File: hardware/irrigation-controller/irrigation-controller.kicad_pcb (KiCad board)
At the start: 2 copper layers, 109 x 71.6 mm, 84 parts, among them J1 RS485, J10 I2C, J11 IO, J12 RELAY_2, J15 FLOW_1, J2 I2C, J3 ICSP, J4 UART, J5 RF Module, J6 PWR 24V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

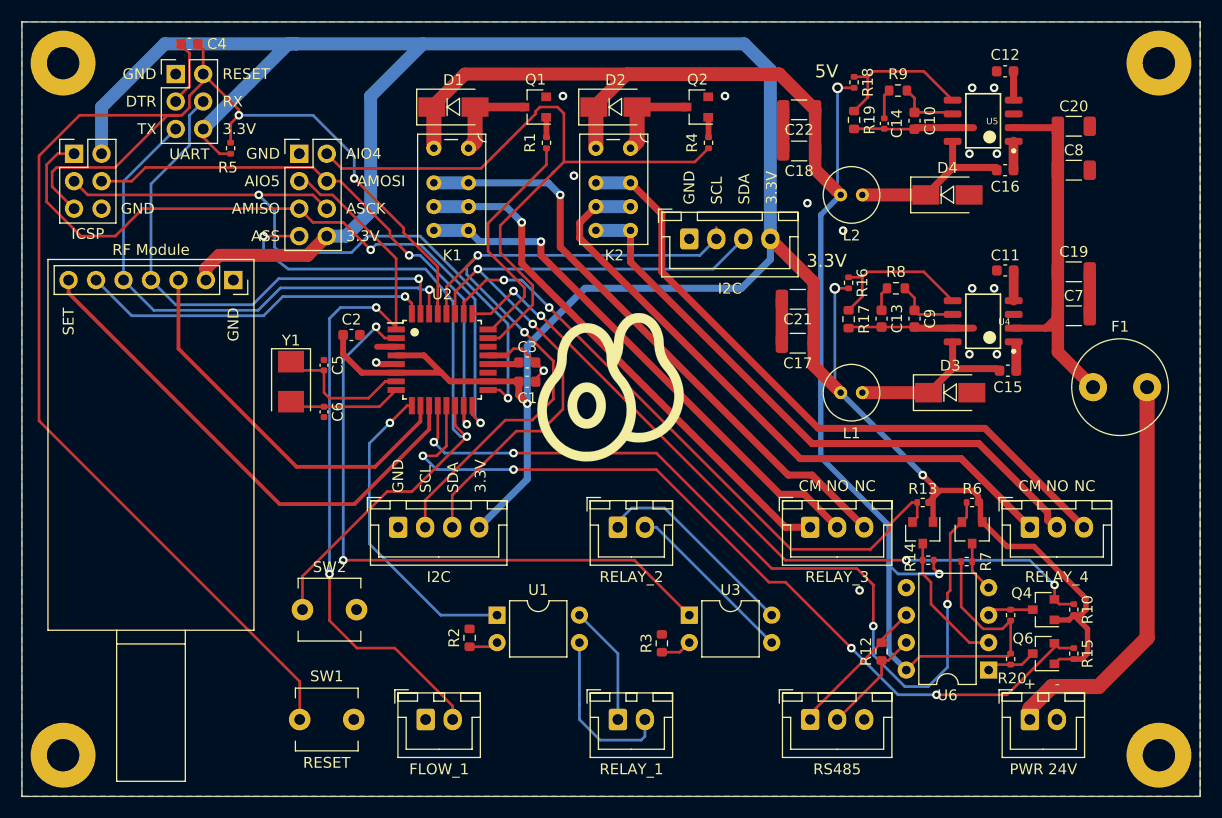
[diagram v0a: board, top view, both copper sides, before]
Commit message: Controller board cosmetic changes
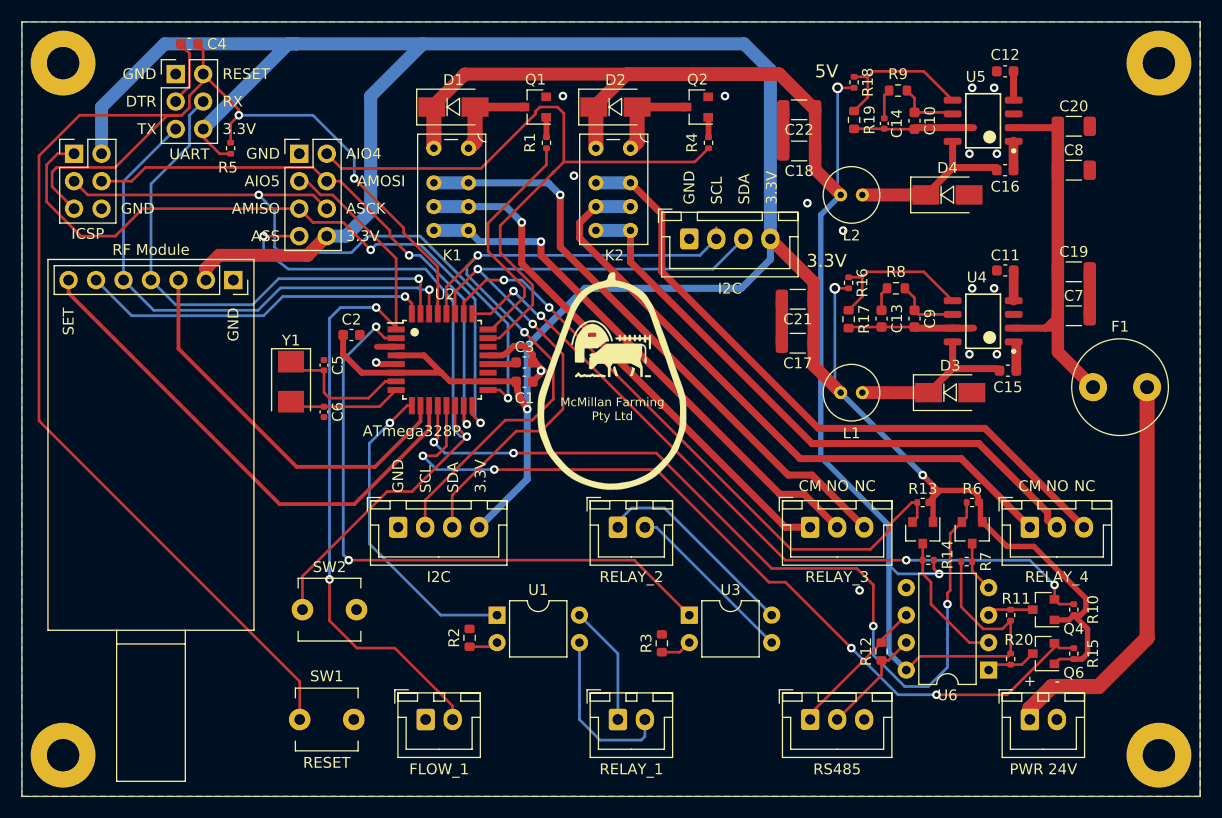
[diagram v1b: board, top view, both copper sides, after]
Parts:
- U2: value ATmega328P-AU -> ATmega328P
- moved G*** 0.57 mm to (106.3, 111.0)
- moved C1 0.25 mm to (98.0, 111.0)
- moved C3 0.25 mm to (98.0, 109.2)
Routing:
- net GND: track 45.7 -> 46.4 mm
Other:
- board text added: "Daniel McMillan 2021"
- board text added: "McMillan Farming Pty Ltd"
- board text removed: "Designed by Daniel McMillan - 2021"

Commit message: Add remote unit board
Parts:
- J5: footprint Connector_PinSocket_2.54mm:PinSocket_1x07_P2.54mm_Vertical -> lib:YL_800T
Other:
- board text removed: "McMillan Farming Pty Ltd"

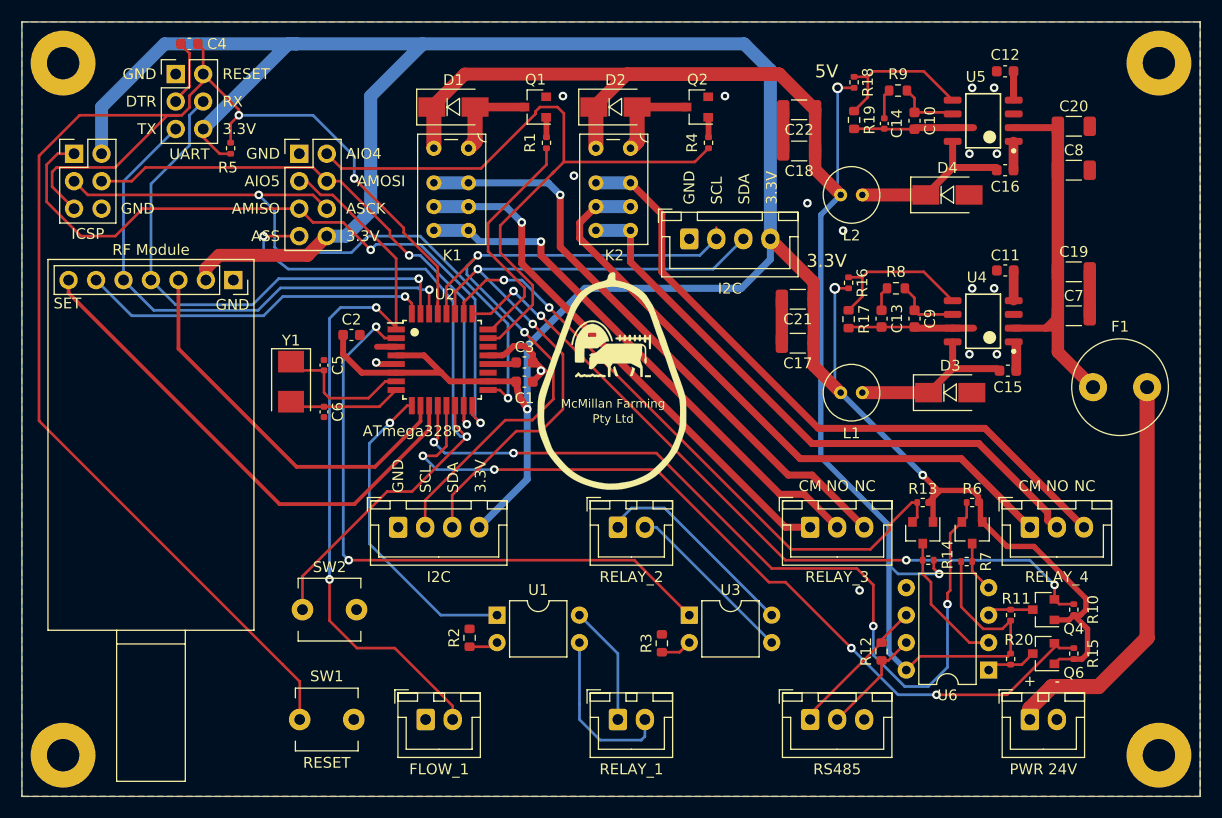
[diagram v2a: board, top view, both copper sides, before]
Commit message: Update irrigation controller board
Remove atmega328p
Remove 5v voltage regulator
Replace max485 with max3485
Remove signal relays
Add female headers for ESP32
Add two LEDs
Update BOM based on JLCPCB availability
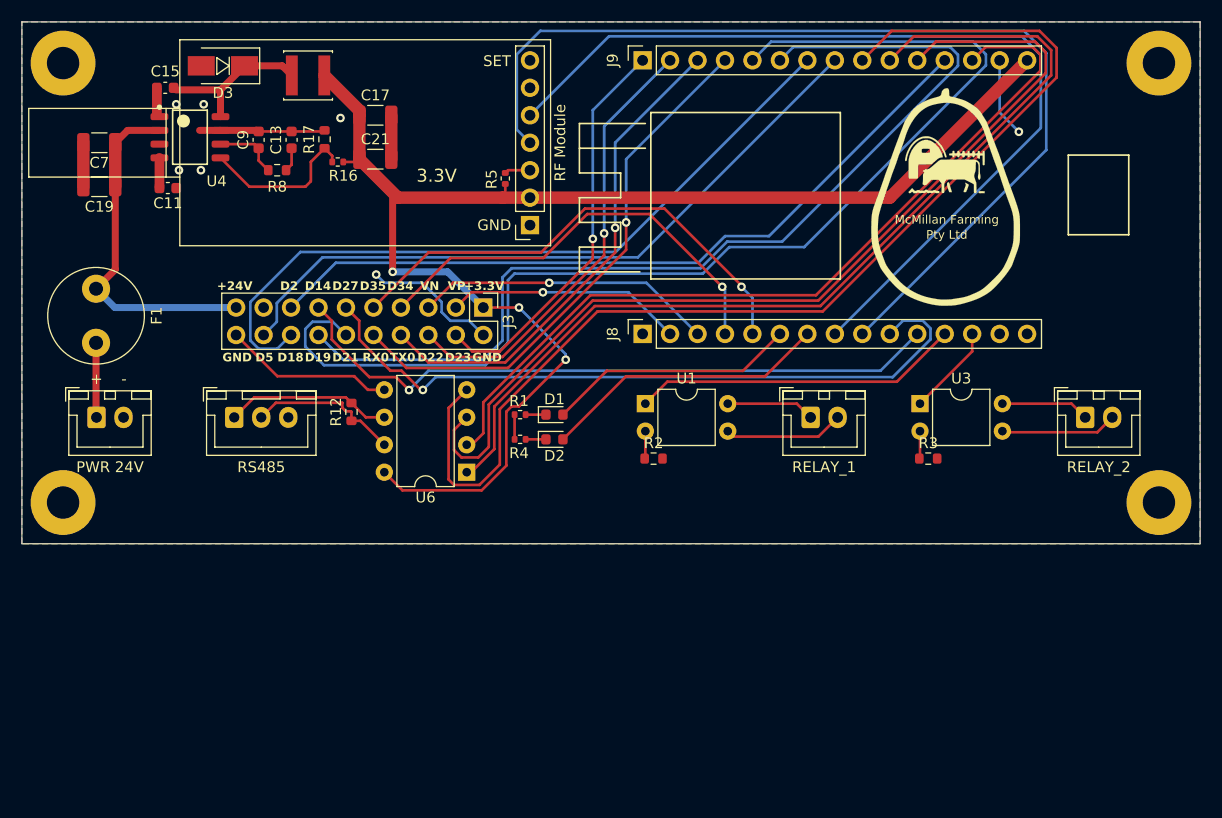
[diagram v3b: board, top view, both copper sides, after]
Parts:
- removed C1, C16, C2, C3, C4: 100nF, Capacitor_SMD:C_0603_1608Metric
- removed C10: 15pF, Capacitor_SMD:C_0603_1608Metric
- removed C12: 8.2nF, Capacitor_SMD:C_0603_1608Metric
- removed C14: 1.5nF, Capacitor_SMD:C_0402_1005Metric
- removed C18, C20, C22, C8: 10uF, Capacitor_SMD:C_1206_3216Metric
- removed C5, C6: 22pF, Capacitor_SMD:C_0402_1005Metric
- removed D4: 550mV 1A, Diode_SMD:D_SMA
- removed J10, J2: I2C, Connector_JST:JST_XH_B4B-XH-A_1x04_P2.50mm_Vertical
- removed J11: IO, Connector_PinHeader_2.54mm:PinHeader_2x04_P2.54mm_Vertical
- removed J15: FLOW_1, Connector_JST:JST_XH_B2B-XH-A_1x02_P2.50mm_Vertical
- removed J4: UART, Connector_PinHeader_2.54mm:PinHeader_2x03_P2.54mm_Vertical
- removed K1: RELAY_3, lib:Relay_DPDT_NEXEM_UA2_Pitch3.2mm
- removed K2: RELAY_4, lib:Relay_DPDT_NEXEM_UA2_Pitch3.2mm
- removed L2: 4.7uH, Capacitor_THT:C_Radial_D5.0mm_H5.0mm_P2.00mm
- removed Q1, Q2: MMBT3904, Package_TO_SOT_SMD:SOT-23
- removed Q3, Q4, Q5, Q6: 2N7002, Package_TO_SOT_SMD:SOT-23
- removed R10, R11, R13, R14, R15, R18, R20, R6, R7: 10k, Resistor_SMD:R_0402_1005Metric
- removed R19: 1.8k, Resistor_SMD:R_0603_1608Metric
- removed R9: 20k, Resistor_SMD:R_0603_1608Metric
- removed SW1: RESET, lib:SW_SPST_THT_5.0mm
- removed SW2: BUTTON, lib:SW_SPST_THT_5.0mm
- removed U2: ATmega328P, Package_QFP:TQFP-32_7x7mm_P0.8mm
- removed U5: TPS54331DR, TPS54331DR:Texas_Instruments-TPS54331DR-Level_A
- removed Y1: 8MHz, Crystal:Crystal_SMD_5032-2Pin_5.0x3.2mm
- C13: value 2.7nF -> 2.2nF
- C9: value 27pF -> 22pF
- D1, D2: value 1.1V 1A -> LED; footprint Diode_SMD:D_SMA -> LED_SMD:LED_0603_1608Metric
- F1: value Fuse -> 200mA
- J3: value ICSP -> I/O; footprint Connector_PinHeader_2.54mm:PinHeader_2x03_P2.54mm_Vertical -> Connector_PinHeader_2.54mm:PinHeader_2x10_P2.54mm_Vertical
- J8: value RELAY_3 -> ESP32; footprint Connector_JST:JST_XH_B3B-XH-A_1x03_P2.50mm_Vertical -> Connector_PinSocket_2.54mm:PinSocket_1x15_P2.54mm_Vertical
- J9: value RELAY_4 -> ESP32; footprint Connector_JST:JST_XH_B3B-XH-A_1x03_P2.50mm_Vertical -> Connector_PinSocket_2.54mm:PinSocket_1x15_P2.54mm_Vertical
- L1: footprint Capacitor_THT:C_Radial_D5.0mm_H5.0mm_P2.00mm -> Inductor_SMD:L_Changjiang_FNR4020S
- R1, R4: value 2.2k -> 330
- R2, R3: value 620 -> 560
- U6: value MAX485 -> MAX3485
- moved F1 92.7 mm to (58.4, 102.4), turned to -90 degrees
- moved C7 91.5 mm to (58.7, 88.9), turned to 180 degrees
- moved J6 90.7 mm to (58.5, 114.3)
- moved C19 90.5 mm to (58.7, 93.0), turned to 180 degrees
- moved C15 82.2 mm to (64.8, 83.8), turned to 180 degrees
- moved C11 77.8 mm to (65.1, 93.1), turned to 0 degrees
- moved U4 75.3 mm to (67.1, 88.4), turned to 0 degrees
- moved D3 73.7 mm to (70.2, 81.8), turned to 180 degrees
- moved C9 62.9 mm to (73.5, 88.6), turned to 90 degrees
- moved J1 60.1 mm to (71.2, 114.3)
- moved L1 59.1 mm to (78.0, 82.7), turned to 0 degrees
- moved R8 58.3 mm to (75.2, 91.4), turned to 0 degrees
- moved C13 57.0 mm to (76.5, 88.6), turned to 90 degrees
- moved J9 56.1 mm to (109.0, 81.3), turned to 90 degrees
- moved R12 53.8 mm to (82.0, 113.8)
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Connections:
- net R1A renamed Net-(J7-Pin_1)
- net R1B renamed Net-(J7-Pin_2)
- net R2A renamed Net-(J12-Pin_1)
- net R2B renamed Net-(J12-Pin_2)
- net RS485A renamed Net-(J1-Pin_1)
- net RS485B renamed Net-(J1-Pin_2)
- C17 pad 1: +3V3 -> +3.3V
- C21 pad 1: +3V3 -> +3.3V
- D1 pad 1: +5V -> Net-(D1-K)
- D1 pad 2: Net-(D1-Pad2) -> ED32
- D2 pad 1: +5V -> Net-(D2-K)
- D2 pad 2: Net-(D2-Pad2) -> ED33
- J3 pad 1: AMISO -> +3.3V
- J3 pad 2: +3V3 -> GND
- J3 pad 3: ASCK -> EVP
- J3 pad 4: AMOSI -> ED23
- J3 pad 5: ARESET -> EVN
- J3 pad 6: GND -> ED22
- J5 pad 2: +3V3 -> +3.3V
- J5 pad 3: RFEN -> Net-(J5-Pin_3)
- J5 pad 4: ATXD -> ED26
- J5 pad 5: ARXD -> ED25
- J5 pad 6: RFAUX -> unconnected-(J5-Pin_6-Pad6)
- J5 pad 7: RFSET -> unconnected-(J5-Pin_7-Pad7)
- J8 pad 1: R3AC -> unconnected-(J8-Pin_1-Pad1)
- J8 pad 2: R3ANO -> EVP
- J8 pad 3: R3ANC -> EVN
- J9 pad 1: R4AC -> ED23
- J9 pad 2: R4ANO -> ED22
- J9 pad 3: R4ANC -> ETX0
- L1 pad 2: +3V3 -> +3.3V
- R1 pad 1: Net-(Q1-Pad1) -> Net-(D1-K)
- R1 pad 2: AIO3 -> GND
- R16 pad 1: +3V3 -> +3.3V
- R4 pad 1: Net-(Q2-Pad1) -> Net-(D2-K)
- R4 pad 2: AIO4 -> GND
- R5 pad 1: +3V3 -> Net-(J5-Pin_3)
- R5 pad 2: ARESET -> +3.3V
- U1 pad 1: AIO1 -> ED12
- U3 pad 1: AIO2 -> ED13
- U4 pad 3: Net-(U4-Pad3) -> unconnected-(U4-EN-Pad3)
- U6 pad 1: Net-(Q6-Pad3) -> ERX2
- U6 pad 2: Net-(Q5-Pad3) -> ED15
- U6 pad 3: Net-(Q4-Pad3) -> ED4
- U6 pad 4: Net-(Q3-Pad3) -> ETX2
- U6 pad 8: +5V -> +3.3V
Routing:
- net +3V3: track 287.1 -> 0.00 mm, vias 3 -> 0
- net +5V: track 163.3 -> 0.00 mm, vias 2 -> 0
- net ARESET: track 142.3 -> 0.00 mm, vias 2 -> 0
- net +3.3V: track 0.00 -> 137.3 mm, vias 0 -> 3
- net ED21: track 0.00 -> 108.5 mm
- net ETX2: track 0.00 -> 106.5 mm
- net ED19: track 0.00 -> 93.0 mm
- net ED26: track 0.00 -> 92.4 mm
- net ED4: track 0.00 -> 90.5 mm
- net ERX2: track 0.00 -> 90.3 mm
- net ED25: track 0.00 -> 84.7 mm
- net ASTX: track 80.9 -> 0.00 mm, vias 4 -> 0
- net ASRX: track 78.0 -> 0.00 mm, vias 4 -> 0
- net ED15: track 0.00 -> 77.7 mm
- net ED2: track 0.00 -> 69.9 mm
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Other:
- board size 109 x 71.6 mm -> 109 x 48.3 mm
- net class Default removed
- board text added: "+24V"
- board text added: "+3.3V"
- board text added: "D14"
- board text added: "D18"
- board text added: "D19"
- board text added: "D2"
- board text added: "D21"
- board text added: "D22"
- board text added: "D23"
- board text added: "D27"
- board text added: "D34"
- board text added: "D35"
- board text added: "D5"
- board text added: "Daniel McMillan 2023"
- board text added: "GND"
- board text added: "RX0"
- board text added: "TX0"
- board text added: "VN"
- board text added: "VP"
- board text removed: "5V"
- board text removed: "Daniel McMillan 2021"

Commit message: Update remote unit PCB
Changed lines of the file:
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@@
     (property "ki_keywords" "connector")
     (attr through_hole)
-    (fp_text reference "J5" (at 0 -2.77) (layer "F.Fab")
-        (effects (font (size 1 1) (thickness 0.15)))
-    )
-    (fp_text value "RF Module" (at -2.794 7.62 90) (layer "F.SilkS")
-        (effects (font (size 1 1) (thickness 0.15)))
-    )
-    (fp_text user "SET" (at 3.048 15.1725) (layer "F.SilkS")
-        (effects (font (size 1 1) (thickness 0.15)))
-    )
-    (fp_text user "GND" (at 3.302 0) (layer "F.SilkS")
-        (effects (font (size 1 1) (thickness 0.15)))
-    )
-    (fp_text user "${REFERENCE}" (at 0 7.62 90) (layer "F.Fab")
+    (fp_text reference "J5" (at 0 -2.77 180) (layer "F.Fab")
+        (effects (font (size 1 1) (thickness 0.15)))
+    )
+    (fp_text value "RF Module" (at -2.794 7.62 -90) (layer "F.SilkS")
+        (effects (font (size 1 1) (thickness 0.15)))
+    )
+    (fp_text user "TXD" (at 4.552 10.16 180) (layer "F.SilkS")
+        (effects (font (size 1 1) (thickness 0.15)) (justify left))
+    )
+    (fp_text user "GND" (at 4.552 0 180) (layer "F.SilkS")
+        (effects (font (size 1 1) (thickness 0.15)) (justify left))
+    )
+    (fp_text user "AUX" (at 4.552 12.7 180) (layer "F.SilkS")
+        (effects (font (size 1 1) (thickness 0.15)) (justify left))
+    )
+    (fp_text user "VCC" (at 4.552 2.52 180) (layer "F.SilkS")
+        (effects (font (size 1 1) (thickness 0.15)) (justify left))
+    )
+    (fp_text user "SET" (at 4.552 15.1725 180) (layer "F.SilkS")
+        (effects (font (size 1 1) (thickness 0.15)) (justify left))
+    )
+    (fp_text user "RXD" (at 4.552 7.62 180) (layer "F.SilkS")
+        (effects (font (size 1 1) (thickness 0.15)) (justify left))
+    )
+    (fp_text user "EN" (at 4.552 5.08 180) (layer "F.SilkS")
+        (effects (font (size 1 1) (thickness 0.15)) (justify left))
+    )
+    (fp_text user "${REFERENCE}" (at 0 7.62 -90) (layer "F.Fab")
         (effects (font (size 1 1) (thickness 0.15)))
     )
@@
     (property "ki_keywords" "R res resistor")
     (attr smd)
-    (fp_text reference "R5" (at 0.072 1.27 90) (layer "F.SilkS")
-        (effects (font (size 1 1) (thickness 0.15)))
-    )
+    (fp_text reference "R5" (at 0.3048 2.7432 90) (layer "F.SilkS")
+        (effects (font (size 1 1) (thickness 0.15)))
+    )
